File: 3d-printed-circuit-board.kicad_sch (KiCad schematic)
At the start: 8 parts

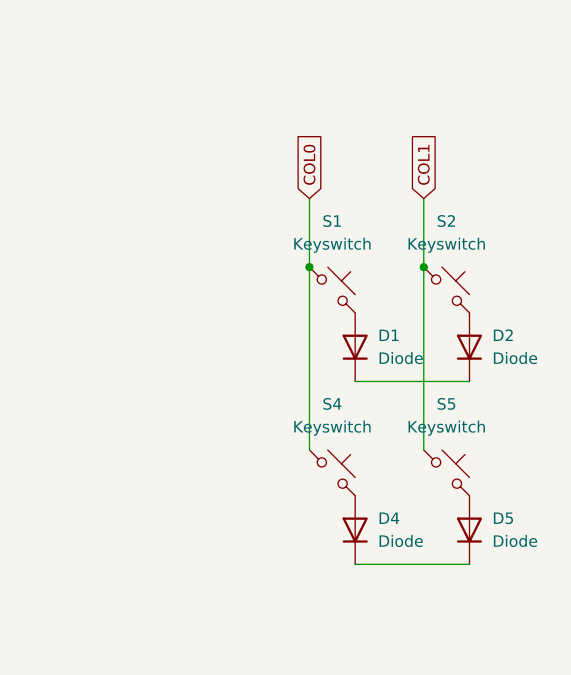
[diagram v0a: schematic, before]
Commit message: Add column stagger
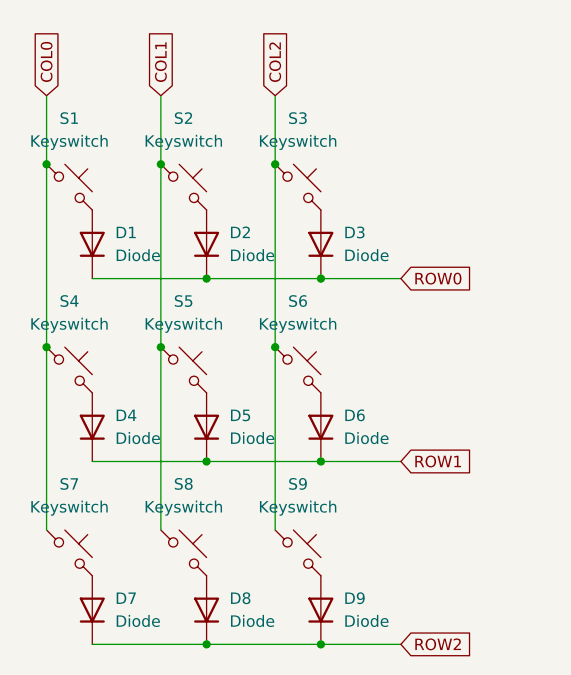
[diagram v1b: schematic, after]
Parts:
- added D3, D6, D7, D8, D9: Diode, ScottoKeebs_Components:Diode_DO-35, symbol ScottoKeebs:Placeholder_Diode
- added S3, S6, S7, S8, S9: Keyswitch, ScottoKeebs_MX:MX_PCB_1.00u, symbol ScottoKeebs:Placeholder_Keyswitch
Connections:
- net COL0: now also S7.1
- net COL1: now also S8.1
- net ROW0: now reaches D1.1 (K), D2.1 (K)
- net ROW0: now also D3.1 (K)
- net ROW1: now reaches D4.1 (K), D5.1 (K)
- net ROW1: now also D6.1 (K)
- new net: D7.2 (A), S7.2
- new net: D3.2 (A), S3.2
- new net: D8.2 (A), S8.2
- new net: D9.2 (A), S9.2
- new net: D6.2 (A), S6.2
- new net COL2: S3.1, S6.1, S9.1
- new net ROW2: D7.1 (K), D8.1 (K), D9.1 (K)
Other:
- moved on the sheet: D1, D2, D4, D5, S1, S2, S4, S5

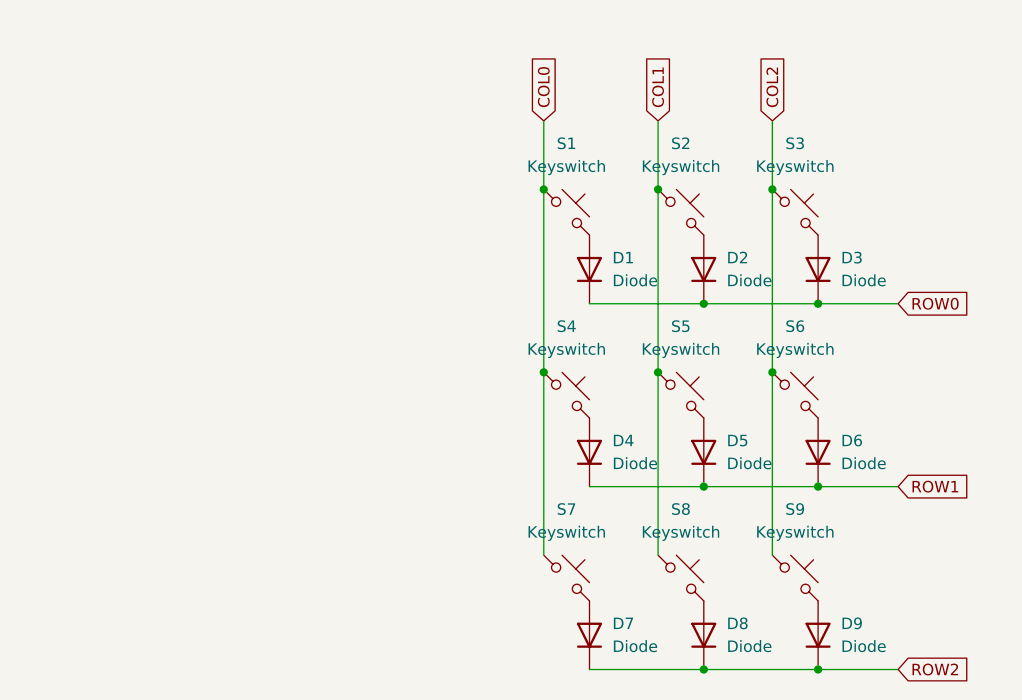
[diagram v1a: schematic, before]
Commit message: Add MCU footprint
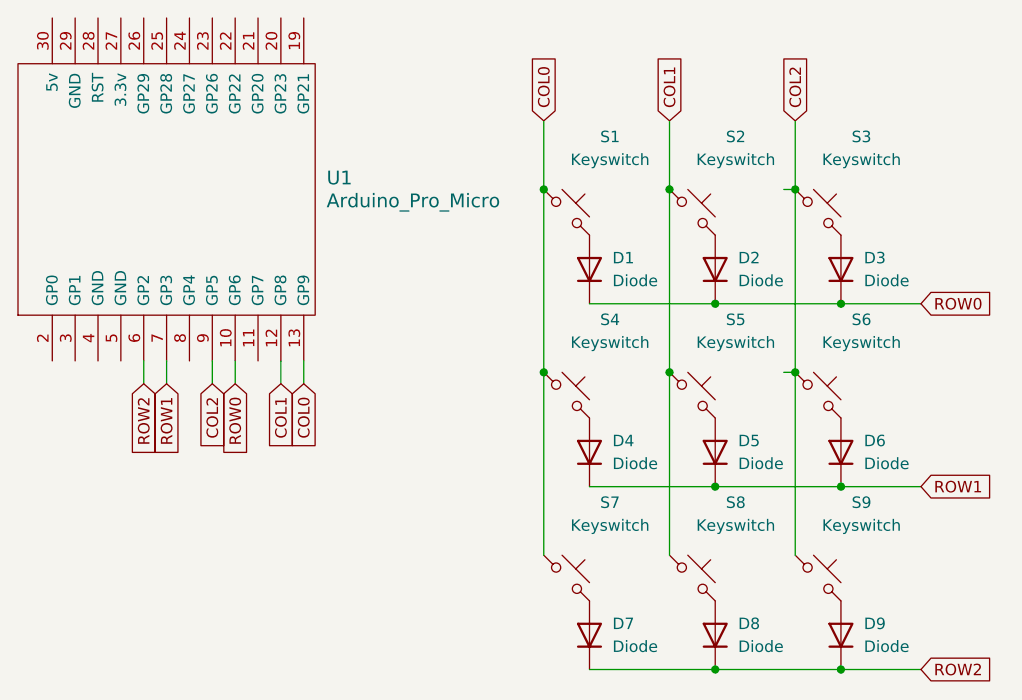
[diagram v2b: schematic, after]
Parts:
- removed D9: Diode, ScottoKeebs_Components:Diode_DO-35, symbol ScottoKeebs:Placeholder_Diode
- removed S9: Keyswitch, ScottoKeebs_MX:MX_PCB_1.00u, symbol ScottoKeebs:Placeholder_Keyswitch
- added D8: Diode, ScottoKeebs_Components:Diode_DO-35, symbol ScottoKeebs:Placeholder_Diode
- added S8: Keyswitch, ScottoKeebs_MX:MX_PCB_1.00u, symbol ScottoKeebs:Placeholder_Keyswitch
- added U1: Arduino_Pro_Micro, ScottoKeebs_MCU:RP2040_Pro_Micro_Custom, symbol ScottoKeebs:MCU_RP2040_Pro_Micro_Custom
- renumbered D8 to D9, S8 to S9
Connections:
- net COL0: now also U1.13 (GP9)
- net COL1: now also S8.1, U1.12 (GP8); no longer S9.1
- net COL2: now also S9.1, U1.9 (GP5)
- net ROW0: now also U1.10 (GP6)
- net ROW1: now also U1.7 (GP3)
- net ROW2: now also D8.1 (K), U1.6 (GP2)
- new net: D8.2 (A), S8.2
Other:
- moved on the sheet: D2, D3, D5, D6, D9, S2, S3, S5, S6, S9

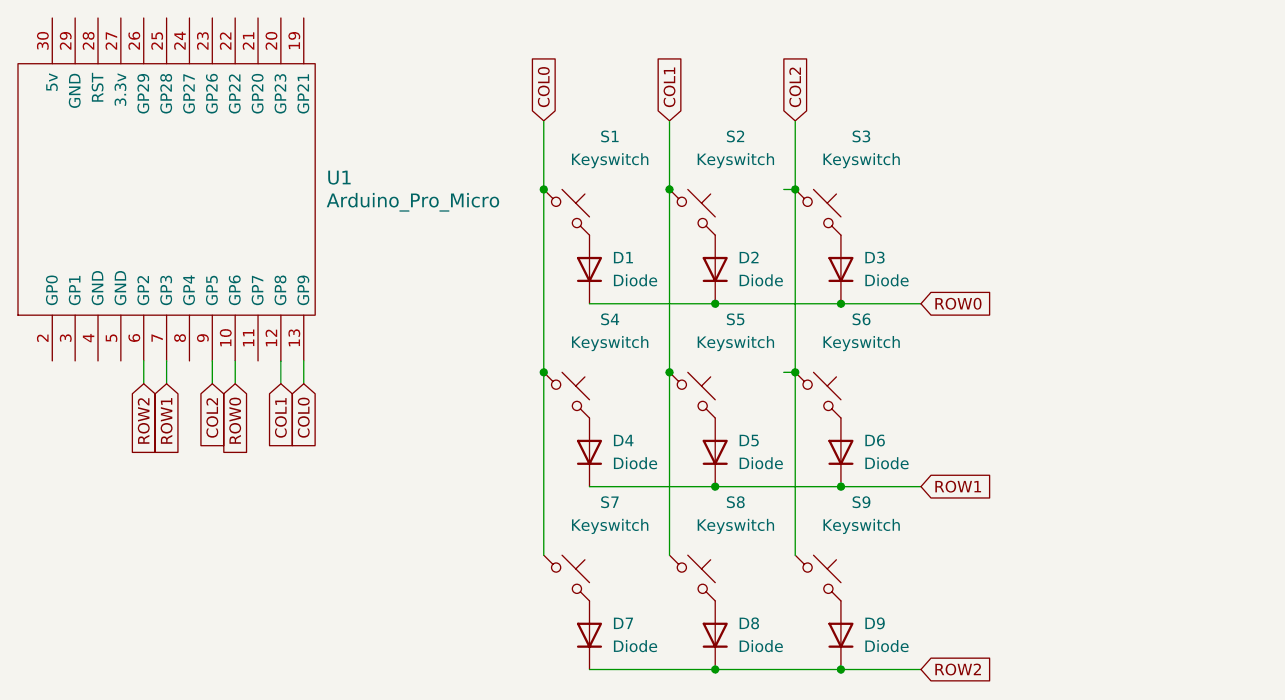
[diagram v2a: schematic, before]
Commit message: Revise routing to reduce solder points
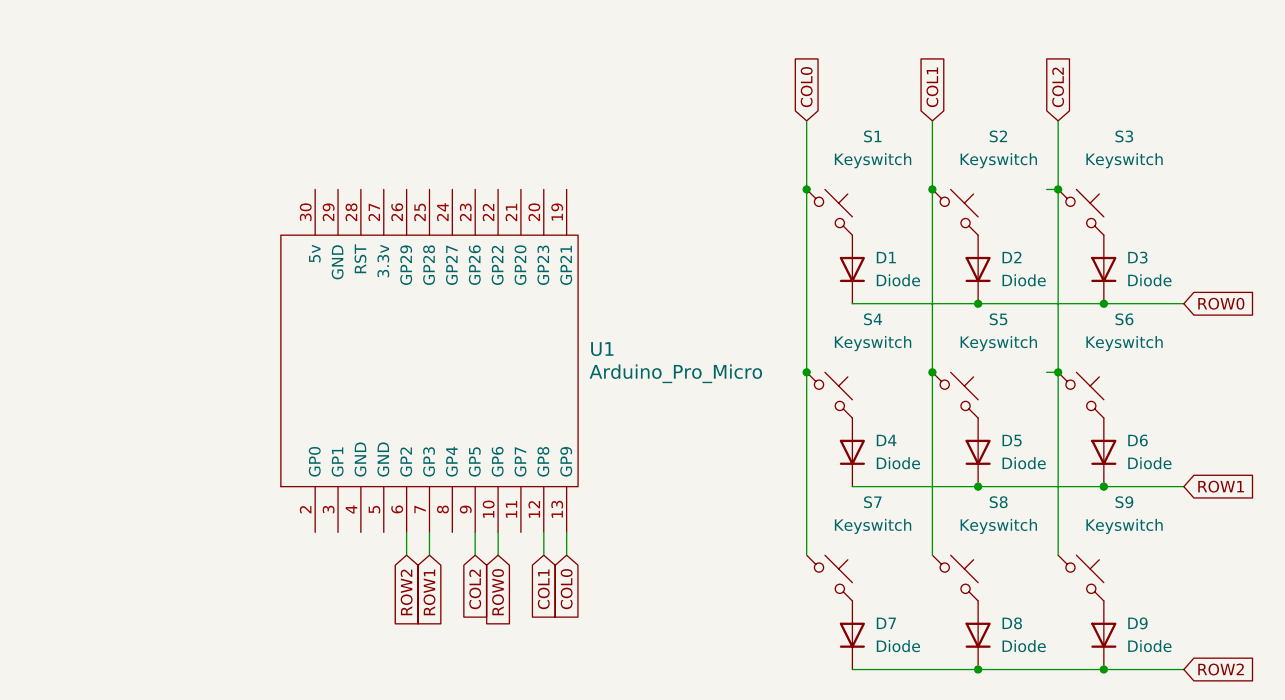
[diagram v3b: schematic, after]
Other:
- moved on the sheet: D1, D2, D3, D4, D5, D6, D7, D8, D9, S1, S2, S3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

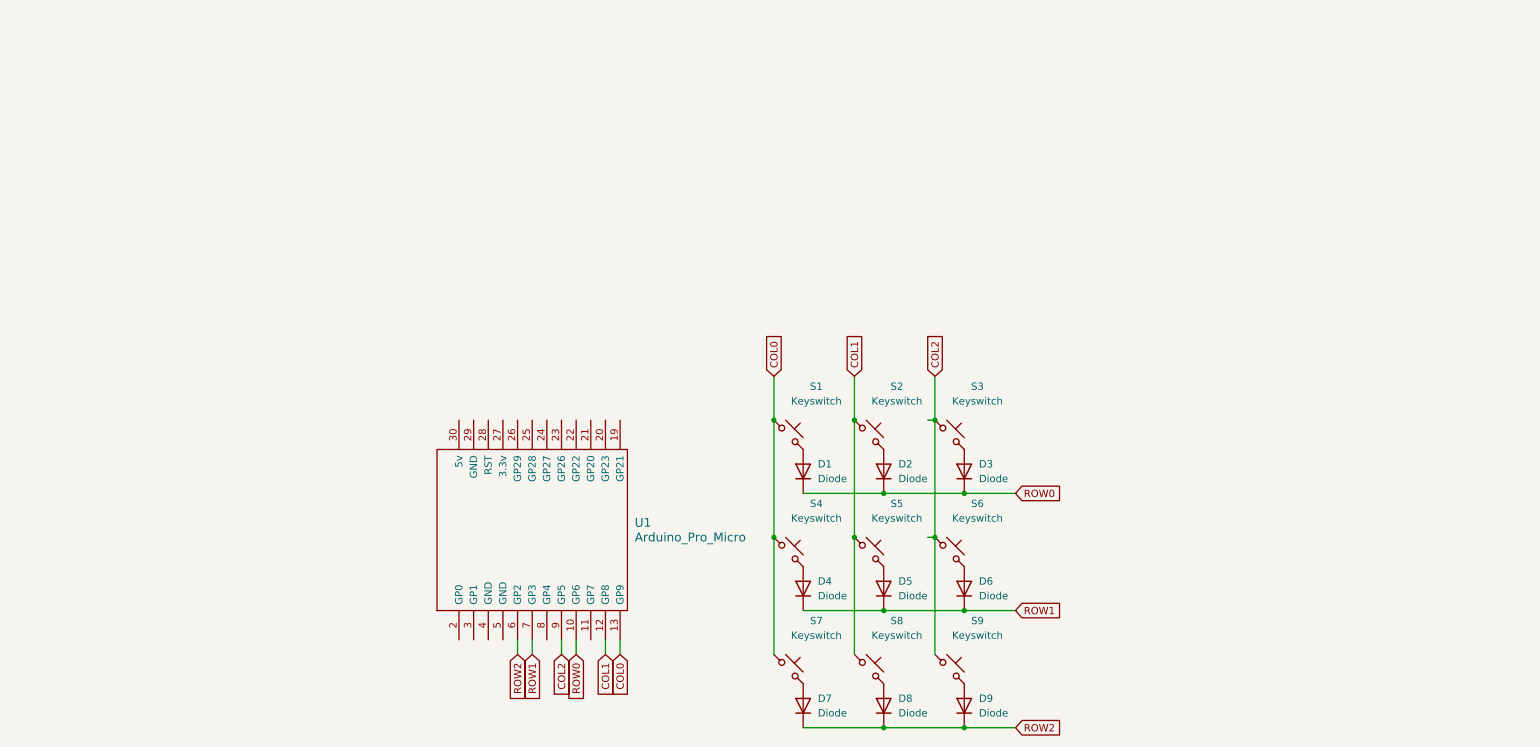
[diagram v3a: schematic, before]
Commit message: Route full hhkb layout
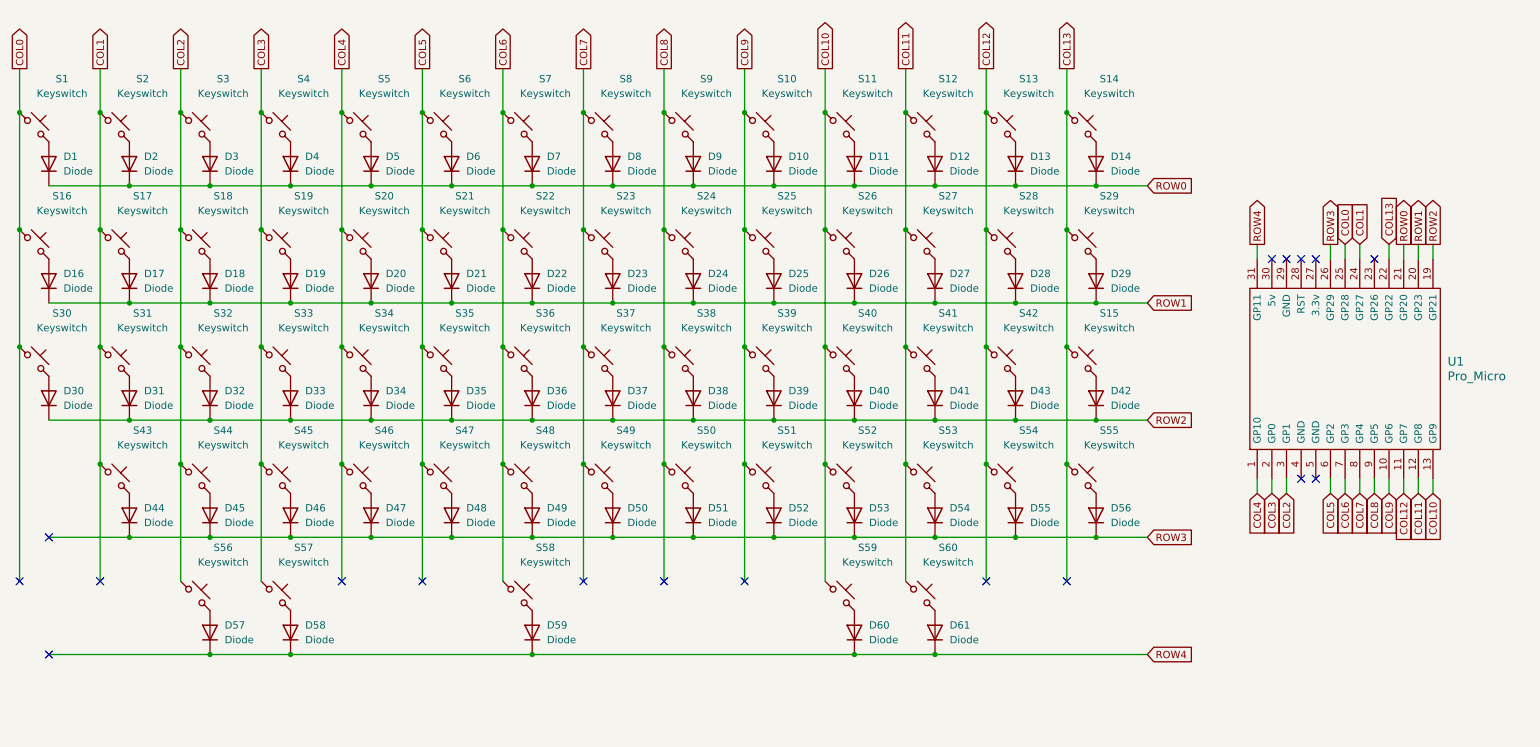
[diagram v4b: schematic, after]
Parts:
- added D10, D11, D12, D13, D14, D19, D20, D21, D22, D23, D24, D25, D26, D27, D28, D29, D30, D31, D32, D33, D34, D35, D36, D37, D38, D39, D4, D40, D41, D42, D43, D44, D45, D46, D47, D48, D49, D5, D50, D51, D52, D53, D54, D55, D56, D57, D58, D59, D6, D60, D61: Diode, ScottoKeebs_Components:Diode_DO-35, symbol ScottoKeebs:Placeholder_Diode
- added S10, S11, S12, S13, S14, S15, S19, S20, S21, S22, S23, S24, S25, S26, S27, S28, S29, S30, S31, S32, S33, S34, S35, S36, S37, S38, S39, S4, S40, S41, S42, S43, S44, S45, S46, S47, S48, S49, S5, S50, S51, S52, S53, S54, S55, S56, S57, S58, S59, S6, S60: Keyswitch, ScottoKeebs_MX:MX_PCB_1.00u, symbol ScottoKeebs:Placeholder_Keyswitch
- U1: value Arduino_Pro_Micro -> Pro_Micro; footprint ScottoKeebs_MCU:RP2040_Pro_Micro_Custom -> ScottoKeebs_MCU:RP2040_Pro_Micro; symbol ScottoKeebs:MCU_RP2040_Pro_Micro_Custom -> ScottoKeebs:MCU_RP2040_Pro_Micro
- renumbered D4 to D16, D5 to D17, D6 to D18, S4 to S16, S5 to S17, S6 to S18
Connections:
- net COL0: now also U1.25 (GP28), S30.1; no longer S7.1, U1.13 (GP9)
- net COL1: now also U1.24 (GP27), S31.1, S43.1; no longer S8.1, U1.12 (GP8)
- net COL2: now also U1.3 (GP1), S32.1, S44.1, S56.1; no longer S9.1, U1.9 (GP5)
- net ROW0: now also D7.1 (K), D8.1 (K), D9.1 (K), U1.21 (GP20), D10.1 (K), D11.1 (K), D12.1 (K), D13.1 (K), D14.1 (K), D4.1 (K), D5.1 (K), D6.1 (K); no longer U1.10 (GP6)
- net ROW1: now also U1.20 (GP23), D19.1 (K), D20.1 (K), D21.1 (K), D22.1 (K), D23.1 (K), D24.1 (K), D25.1 (K), D26.1 (K), D27.1 (K), D28.1 (K), D29.1 (K); no longer U1.7 (GP3)
- net ROW2: now also U1.19 (GP21), D30.1 (K), D31.1 (K), D32.1 (K), D33.1 (K), D34.1 (K), D35.1 (K), D36.1 (K), D37.1 (K), D38.1 (K), D39.1 (K), D40.1 (K), D41.1 (K), D42.1 (K), D43.1 (K); no longer D7.1 (K), D8.1 (K), D9.1 (K), U1.6 (GP2)
- net COL12: now reaches U1.11 (GP7)
- net COL12: now also S13.1, S28.1, S42.1, S54.1
- net COL3: now reaches U1.2 (GP0)
- net COL3: now also S19.1, S33.1, S4.1, S45.1, S57.1
- net COL13: now reaches U1.22 (GP22)
- net COL13: now also S14.1, S15.1, S29.1, S55.1
- net ROW3: now reaches U1.26 (GP29)
- net ROW3: now also D44.1 (K), D45.1 (K), D46.1 (K), D47.1 (K), D48.1 (K), D49.1 (K), D50.1 (K), D51.1 (K), D52.1 (K), D53.1 (K), D54.1 (K), D55.1 (K), D56.1 (K)
- net COL7: now reaches U1.8 (GP4)
- net COL7: now also S8.1, S23.1, S37.1, S49.1
- new net: D44.2 (A), S43.2
- new net: D14.2 (A), S14.2
- new net: D48.2 (A), S47.2
- new net: D60.2 (A), S59.2
- new net: D49.2 (A), S48.2
- new net: D31.2 (A), S31.2
- new net: D19.2 (A), S19.2
- new net: D59.2 (A), S58.2
- new net: D43.2 (A), S42.2
- new net: D27.2 (A), S27.2
- new net: D10.2 (A), S10.2
- new net: D20.2 (A), S20.2
- new net: D55.2 (A), S54.2
- new net: D53.2 (A), S52.2
- new net: D50.2 (A), S49.2
- new net: D6.2 (A), S6.2
- new net: D37.2 (A), S37.2
- new net: D39.2 (A), S39.2
- new net: D57.2 (A), S56.2
- new net: D23.2 (A), S23.2
- new net: D51.2 (A), S50.2
- new net: D45.2 (A), S44.2
- new net: D32.2 (A), S32.2
- new net: D47.2 (A), S46.2
- new net: D33.2 (A), S33.2
- new net: D29.2 (A), S29.2
- new net: D4.2 (A), S4.2
- new net: D42.2 (A), S15.2
- new net: D52.2 (A), S51.2
- new net: D35.2 (A), S35.2
- new net: D56.2 (A), S55.2
- new net: D13.2 (A), S13.2
- new net: D22.2 (A), S22.2
- new net: D38.2 (A), S38.2
- new net: D24.2 (A), S24.2
- new net: D41.2 (A), S41.2
- new net: D30.2 (A), S30.2
- new net: D26.2 (A), S26.2
- new net: D36.2 (A), S36.2
- new net: D40.2 (A), S40.2
- new net: D28.2 (A), S28.2
- new net: D54.2 (A), S53.2
- new net: D46.2 (A), S45.2
- new net: D21.2 (A), S21.2
- new net: D61.2 (A), S60.2
- new net: D5.2 (A), S5.2
- new net: D11.2 (A), S11.2
- new net: D12.2 (A), S12.2
- new net: D58.2 (A), S57.2
- new net: D34.2 (A), S34.2
- new net: D25.2 (A), S25.2
- new net COL10: S11.1, S26.1, S40.1, S52.1, S59.1, U1.13 (GP9)
- new net COL11: S12.1, S27.1, S41.1, S53.1, S60.1, U1.12 (GP8)
- new net COL4: S20.1, S34.1, S46.1, S5.1, U1.1 (GP10)
- new net COL5: S21.1, S35.1, S47.1, S6.1, U1.6 (GP2)
- new net COL6: S22.1, S36.1, S48.1, S58.1, S7.1, U1.7 (GP3)
- new net COL8: S24.1, S38.1, S50.1, S9.1, U1.9 (GP5)
- new net COL9: S10.1, S25.1, S39.1, S51.1, U1.10 (GP6)
- new net ROW4: D57.1 (K), D58.1 (K), D59.1 (K), D60.1 (K), D61.1 (K), U1.31 (GP11)
- no-connect marks 0 -> 18
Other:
- moved on the sheet: D1, D16, D17, D18, D2, D3, S1, S16, S17, S18, S2, S3
